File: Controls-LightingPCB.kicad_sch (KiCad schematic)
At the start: 30 parts, among them J1 PeripheralCANConnector, J2 PeripheralCANConnector, U1 PeripheralSOM

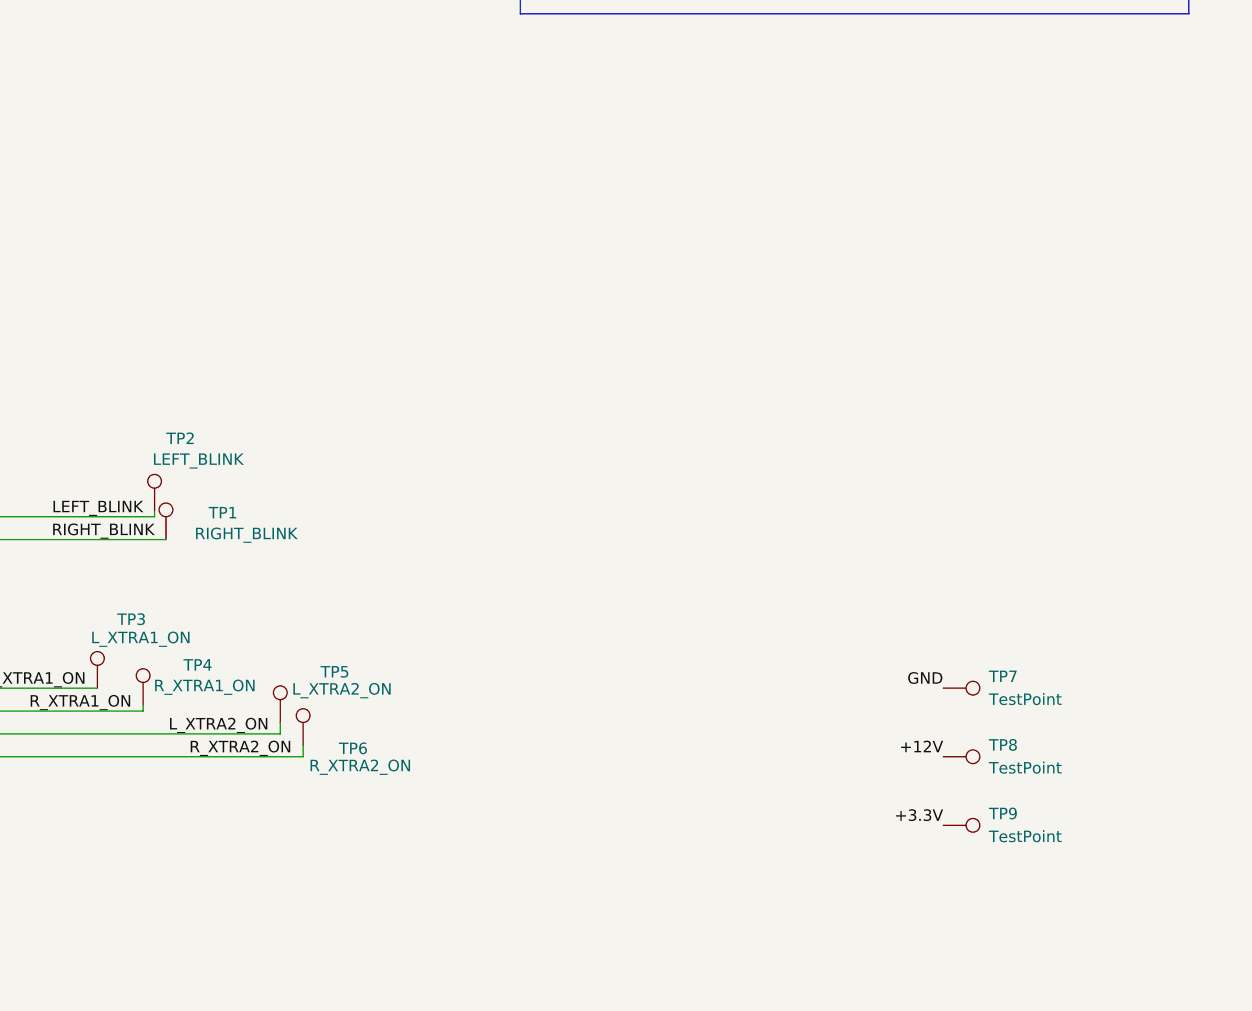
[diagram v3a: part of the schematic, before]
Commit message: added footprints for all components
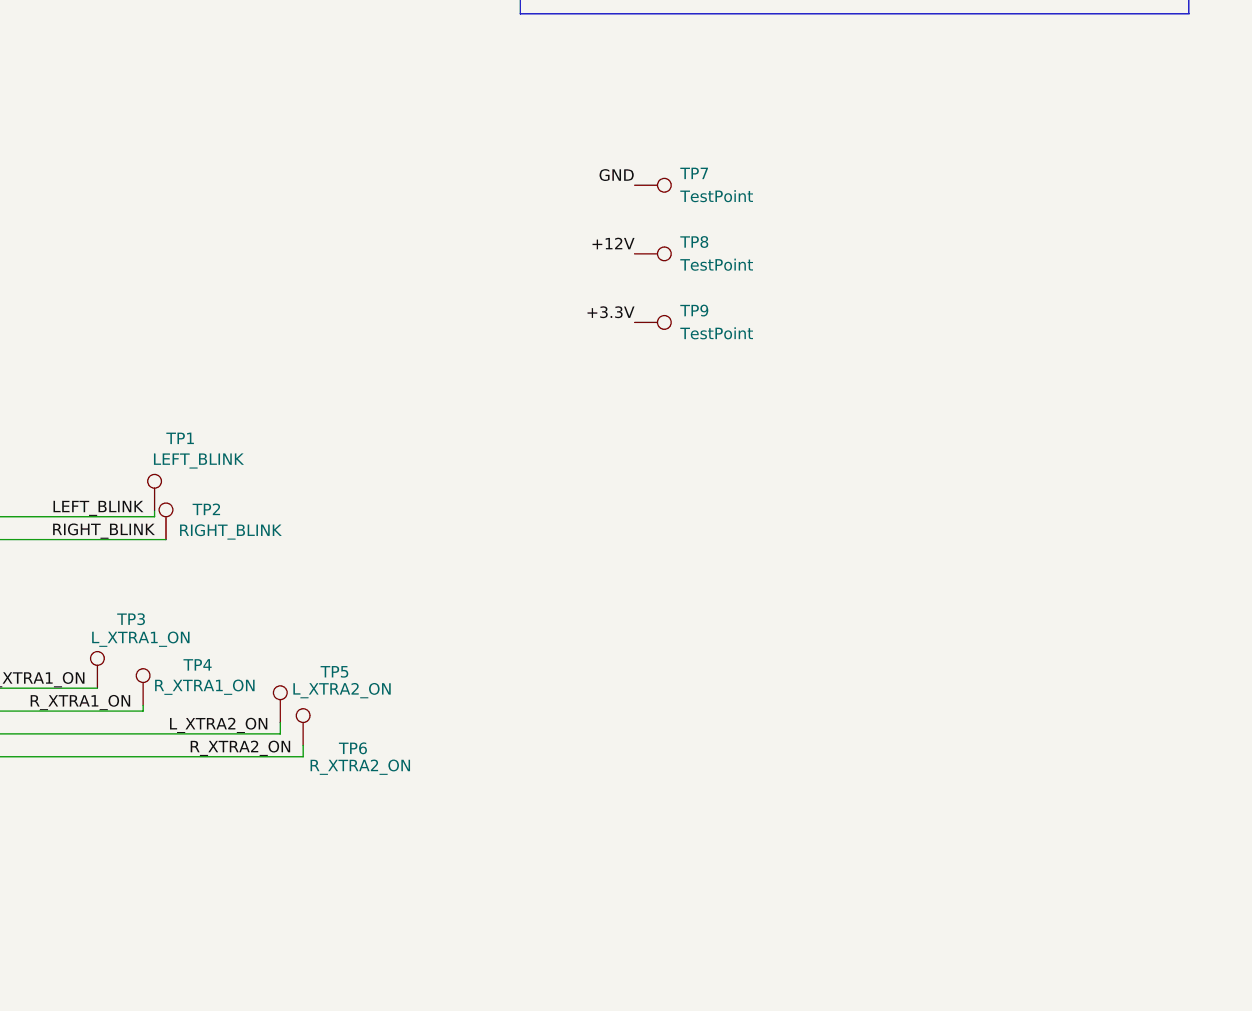
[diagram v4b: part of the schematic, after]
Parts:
- TP1: renamed from TP2; footprint TestPoint:TestPoint_Pad_1.5x1.5mm -> TestPoint:TestPoint_Keystone_5000-5004_Miniature
- TP2: renamed from TP1; footprint TestPoint:TestPoint_Pad_1.5x1.5mm -> TestPoint:TestPoint_Keystone_5000-5004_Miniature
- TP3, TP4, TP5, TP6: footprint TestPoint:TestPoint_Pad_1.5x1.5mm -> TestPoint:TestPoint_Keystone_5000-5004_Miniature
- TP7, TP8, TP9: footprint (none) -> TestPoint:TestPoint_Keystone_5000-5004_Miniature
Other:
- moved on the sheet: TP7, TP8, TP9
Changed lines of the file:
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@@
 	)
 	(label "+3.3V"
-		(at 251.46 140.97 180)
+		(at 217.17 85.09 180)
 		(fields_autoplaced yes)
 		(effects
@@
 	)
 	(label "+12V"
-		(at 251.46 133.35 180)
+		(at 217.17 77.47 180)
 		(fields_autoplaced yes)
 		(effects
@@
 	)
 	(label "GND"
-		(at 251.46 125.73 180)
+		(at 217.17 69.85 180)
 		(fields_autoplaced yes)
 		(effects
@@
 	(symbol
 		(lib_id "Connector:TestPoint")
-		(at 251.46 133.35 270)
+		(at 217.17 77.47 270)
 		(unit 1)
 		(exclude_from_sim no)
@@
 		(fields_autoplaced yes)
 		(property "Reference" "TP8"
-			(at 256.54 132.0799 90)
+			(at 222.25 76.1999 90)
 			(effects
 				(font
@@
 		)
 		(property "Value" "TestPoint"
-			(at 256.54 134.6199 90)
+			(at 222.25 78.7399 90)
 			(effects
 				(font
@@
 			)
 		)
-		(property "Footprint" ""
-			(at 251.46 138.43 0)
-			(effects
-				(font
-					(size 1.27 1.27)
-				)
-				(hide yes)
-			)
-		)
-		(property "Datasheet" "~"
-			(at 251.46 138.43 0)
-			(effects
-				(font
-					(size 1.27 1.27)
-				)
-				(hide yes)
-			)
-		)
-		(property "Description" "test point"
-			(at 251.46 133.35 0)
+		(property "Footprint" "TestPoint:TestPoint_Keystone_5000-5004_Miniature"
+			(at 217.17 82.55 0)
+			(effects
+				(font
+					(size 1.27 1.27)
+				)
+				(hide yes)
+			)
+		)
+		(property "Datasheet" "https://www.keyelco.com/userAssets/file/M65p56.pdf"
+			(at 217.17 82.55 0)
+			(effects
+				(font
+					(size 1.27 1.27)
+				)
+				(hide yes)
+			)
+		)
+		(property "Description" "through-hole test point mini"
+			(at 217.17 77.47 0)
 			(effects
 				(font
@@
 		(on_board yes)
 		(dnp no)
-		(property "Reference" "TP1"
-			(at 171.45 106.2736 0)
+		(property "Reference" "TP2"
+			(at 169.672 105.918 0)
 			(effects
 				(font
@@
 		)
 		(property "Value" "RIGHT_BLINK"
-			(at 173.99 108.585 0)
-			(effects
-				(font
-					(size 1.27 1.27)
-				)
-			)
-		)
-		(property "Footprint" "TestPoint:TestPoint_Pad_1.5x1.5mm"
+			(at 172.212 108.2294 0)
+			(effects
+				(font
+					(size 1.27 1.27)
+				)
+			)
+		)
+		(property "Footprint" "TestPoint:TestPoint_Keystone_5000-5004_Miniature"
 			(at 170.18 109.22 0)
 			(effects
@@
 			)
 		)
-		(property "Datasheet" "~"
+		(property "Datasheet" "https://www.keyelco.com/userAssets/file/M65p56.pdf"
 			(at 170.18 109.22 0)
 			(effects
@@
 			)
 		)
-		(property "Description" ""
+		(property "Description" "through-hole test point mini"
 			(at 165.1 109.22 0)
 			(effects
@@
 			(project "Controls-LightingPCB"
 				(path "/229b82f0-5048-47d6-8bc8-0bcee42eb4bc"
-					(reference "TP1")
+					(reference "TP2")
 					(unit 1)
 				)
@@
 			)
 		)
-		(property "Footprint" "TestPoint:TestPoint_Pad_1.5x1.5mm"
+		(property "Footprint" "TestPoint:TestPoint_Keystone_5000-5004_Miniature"
 			(at 167.64 127.635 0)
 			(effects
@@
 			)
 		)
-		(property "Datasheet" "~"
+		(property "Datasheet" "https://www.keyelco.com/userAssets/file/M65p56.pdf"
 			(at 167.64 127.635 0)
 			(effects
@@
 			)
 		)
-		(property "Description" ""
+		(property "Description" "through-hole test point mini"
 			(at 162.56 127.635 0)
 			(effects
@@
 			)
 		)
-		(property "Footprint" "TestPoint:TestPoint_Pad_1.5x1.5mm"
+		(property "Footprint" "TestPoint:TestPoint_Keystone_5000-5004_Miniature"
 			(at 162.56 125.73 0)
 			(effects
@@
 			)
 		)
-		(property "Datasheet" "~"
+		(property "Datasheet" "https://www.keyelco.com/userAssets/file/M65p56.pdf"
 			(at 162.56 125.73 0)
 			(effects
@@
 			)
 		)
-		(property "Description" ""
+		(property "Description" "through-hole test point mini"
 			(at 157.48 125.73 0)
 			(effects
@@
 		(on_board yes)
 		(dnp no)
-		(property "Reference" "TP2"
+		(property "Reference" "TP1"
 			(at 166.751 98.0186 0)
 			(effects
@@
 			)
 		)
-		(property "Footprint" "TestPoint:TestPoint_Pad_1.5x1.5mm"
+		(property "Footprint" "TestPoint:TestPoint_Keystone_5000-5004_Miniature"
 			(at 168.91 106.045 0)
 			(effects
@@
 			)
 		)
-		(property "Datasheet" "~"
+		(property "Datasheet" "https://www.keyelco.com/userAssets/file/M65p56.pdf"
 			(at 168.91 106.045 0)
 			(effects
@@
 			)
 		)
-		(property "Description" ""
+		(property "Description" "through-hole test point mini"
 			(at 163.83 106.045 0)
 			(effects
@@
 			(project "Controls-LightingPCB"
 				(path "/229b82f0-5048-47d6-8bc8-0bcee42eb4bc"
-					(reference "TP2")
+					(reference "TP1")
 					(unit 1)
 				)
@@
 			)
 		)
-		(property "Footprint" "TestPoint:TestPoint_Pad_1.5x1.5mm"
+		(property "Footprint" "TestPoint:TestPoint_Keystone_5000-5004_Miniature"
 			(at 182.88 129.54 0)
 			(effects
@@
 			)
 		)
-		(property "Datasheet" "~"
+		(property "Datasheet" "https://www.keyelco.com/userAssets/file/M65p56.pdf"
 			(at 182.88 129.54 0)
 			(effects
@@
 			)
 		)
-		(property "Description" ""
+		(property "Description" "through-hole test point mini"
 			(at 177.8 129.54 0)
 			(effects
@@
 	(symbol
 		(lib_id "Connector:TestPoint")
-		(at 251.46 125.73 270)
+		(at 217.17 69.85 270)
 		(unit 1)
 		(exclude_from_sim no)
@@
 		(fields_autoplaced yes)
 		(property "Reference" "TP7"
-			(at 256.54 124.4599 90)
+			(at 222.25 68.5799 90)
 			(effects
 				(font
@@
 		)
 		(property "Value" "TestPoint"
-			(at 256.54 126.9999 90)
+			(at 222.25 71.1199 90)
 			(effects
 				(font
@@
 			)
 		)
-		(property "Footprint" ""
-			(at 251.46 130.81 0)
-			(effects
-				(font
-					(size 1.27 1.27)
-				)
-				(hide yes)
-			)
-		)
-		(property "Datasheet" "~"
-			(at 251.46 130.81 0)
-			(effects
-				(font
-					(size 1.27 1.27)
-				)
-				(hide yes)
-			)
-		)
-		(property "Description" "test point"
-			(at 251.46 125.73 0)
+		(property "Footprint" "TestPoint:TestPoint_Keystone_5000-5004_Miniature"
+			(at 217.17 74.93 0)
+			(effects
+				(font
+					(size 1.27 1.27)
+				)
+				(hide yes)
+			)
+		)
+		(property "Datasheet" "https://www.keyelco.com/userAssets/file/M65p56.pdf"
+			(at 217.17 74.93 0)
+			(effects
+				(font
+					(size 1.27 1.27)
+				)
+				(hide yes)
+			)
+		)
+		(property "Description" "through-hole test point mini"
+			(at 217.17 69.85 0)
 			(effects
 				(font
@@
 	(symbol
 		(lib_id "Connector:TestPoint")
-		(at 251.46 140.97 270)
+		(at 217.17 85.09 270)
 		(unit 1)
 		(exclude_from_sim no)
@@
 		(fields_autoplaced yes)
 		(property "Reference" "TP9"
-			(at 256.54 139.6999 90)
+			(at 222.25 83.8199 90)
 			(effects
 				(font
@@
 		)
 		(property "Value" "TestPoint"
-			(at 256.54 142.2399 90)
+			(at 222.25 86.3599 90)
 			(effects
 				(font
@@
 			)
 		)
-		(property "Footprint" ""
-			(at 251.46 146.05 0)
-			(effects
-				(font
-					(size 1.27 1.27)
-				)
-				(hide yes)
-			)
-		)
-		(property "Datasheet" "~"
-			(at 251.46 146.05 0)
-			(effects
-				(font
-					(size 1.27 1.27)
-				)
-				(hide yes)
-			)
-		)
-		(property "Description" "test point"
-			(at 251.46 140.97 0)
+		(property "Footprint" "TestPoint:TestPoint_Keystone_5000-5004_Miniature"
+			(at 217.17 90.17 0)
+			(effects
+				(font
+					(size 1.27 1.27)
+				)
+				(hide yes)
+			)
+		)
+		(property "Datasheet" "https://www.keyelco.com/userAssets/file/M65p56.pdf"
+			(at 217.17 90.17 0)
+			(effects
+				(font
+					(size 1.27 1.27)
+				)
+				(hide yes)
+			)
+		)
+		(property "Description" "through-hole test point mini"
+			(at 217.17 85.09 0)
 			(effects
 				(font
@@
 			)
 		)
-		(property "Footprint" "TestPoint:TestPoint_Pad_1.5x1.5mm"
+		(property "Footprint" "TestPoint:TestPoint_Keystone_5000-5004_Miniature"
 			(at 185.42 132.08 0)
 			(effects
@@
 			)
 		)
-		(property "Datasheet" "~"
+		(property "Datasheet" "https://www.keyelco.com/userAssets/file/M65p56.pdf"
 			(at 185.42 132.08 0)
 			(effects
@@
 			)
 		)
-		(property "Description" ""
+		(property "Description" "through-hole test point mini"
 			(at 180.34 132.08 0)
 			(effects

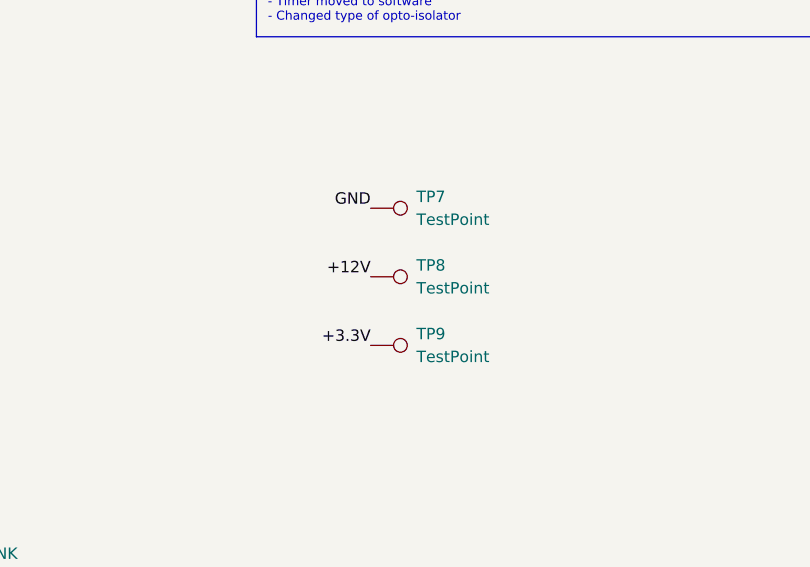
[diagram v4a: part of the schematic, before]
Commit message: changed lights resistor values and updated EL2H7 footprint
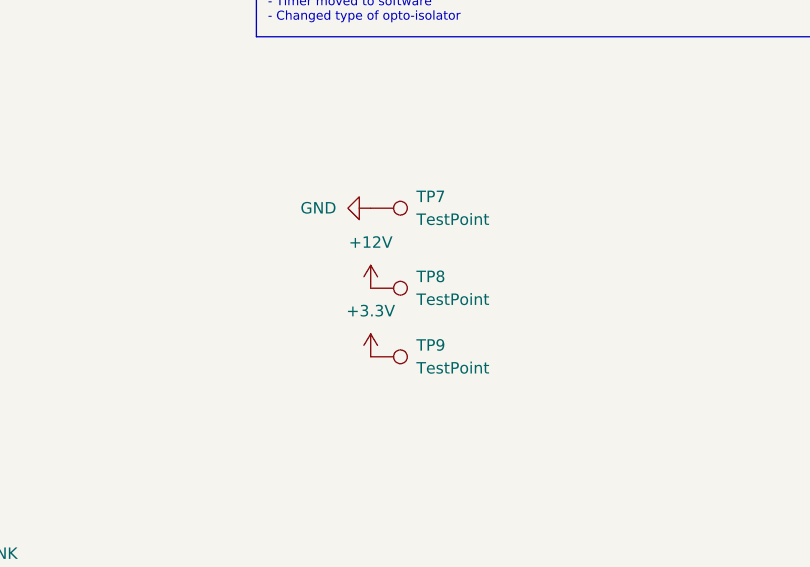
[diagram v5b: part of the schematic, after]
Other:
- moved on the sheet: TP8, TP9
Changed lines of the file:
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@@
 		)
 	)
-	(label "+3.3V"
-		(at 217.17 85.09 180)
-		(fields_autoplaced yes)
-		(effects
-			(font
-				(size 1.27 1.27)
-			)
-			(justify right bottom)
-		)
-	)
-	(label "+12V"
-		(at 217.17 77.47 180)
-		(fields_autoplaced yes)
-		(effects
-			(font
-				(size 1.27 1.27)
-			)
-			(justify right bottom)
-		)
-	)
 	(label "R_XTRA2_ON"
 		(at 179.07 133.35 180)
@@
 		)
 	)
-	(label "GND"
-		(at 217.17 69.85 180)
-		(fields_autoplaced yes)
-		(effects
-			(font
-				(size 1.27 1.27)
-			)
-			(justify right bottom)
-		)
-	)
 	(label "L_XTRA2_ON"
 		(at 96.52 157.48 0)
@@
 	(symbol
 		(lib_id "Connector:TestPoint")
-		(at 217.17 77.47 270)
+		(at 217.17 78.74 270)
 		(unit 1)
 		(exclude_from_sim no)
@@
 		(fields_autoplaced yes)
 		(property "Reference" "TP8"
-			(at 222.25 76.1999 90)
+			(at 222.25 77.4699 90)
 			(effects
 				(font
@@
 		)
 		(property "Value" "TestPoint"
-			(at 222.25 78.7399 90)
+			(at 222.25 80.0099 90)
 			(effects
 				(font
@@
 		)
 		(property "Footprint" "TestPoint:TestPoint_Keystone_5000-5004_Miniature"
-			(at 217.17 82.55 0)
+			(at 217.17 83.82 0)
 			(effects
 				(font
@@
 		)
 		(property "Datasheet" "https://www.keyelco.com/userAssets/file/M65p56.pdf"
-			(at 217.17 82.55 0)
+			(at 217.17 83.82 0)
 			(effects
 				(font
@@
 		)
 		(property "Description" "through-hole test point mini"
-			(at 217.17 77.47 0)
+			(at 217.17 78.74 0)
 			(effects
 				(font
@@
 	)
 	(symbol
+		(lib_id "power:+3.3V")
+		(at 217.17 86.36 0)
+		(unit 1)
+		(exclude_from_sim no)
+		(in_bom yes)
+		(on_board yes)
+		(dnp no)
+		(fields_autoplaced yes)
+		(property "Reference" "#PWR031"
+			(at 217.17 90.17 0)
+			(effects
+				(font
+					(size 1.27 1.27)
+				)
+				(hide yes)
+			)
+		)
+		(property "Value" "+3.3V"
+			(at 217.17 81.28 0)
+			(effects
+				(font
+					(size 1.27 1.27)
+				)
+			)
+		)
+		(property "Footprint" ""
+			(at 217.17 86.36 0)
+			(effects
+				(font
+					(size 1.27 1.27)
+				)
+				(hide yes)
+			)
+		)
+		(property "Datasheet" ""
+			(at 217.17 86.36 0)
+			(effects
+				(font
+					(size 1.27 1.27)
+				)
+				(hide yes)
+			)
+		)
+		(property "Description" "Power symbol creates a global label with name \"+3.3V\""
+			(at 217.17 86.36 0)
+			(effects
+				(font
+					(size 1.27 1.27)
+				)
+				(hide yes)
+			)
+		)
+		(pin "1"
+		)
+		(instances
+			(project ""
+				(path "/229b82f0-5048-47d6-8bc8-0bcee42eb4bc"
+					(reference "#PWR031")
+					(unit 1)
+				)
+			)
+		)
+	)
+	(symbol
 		(lib_id "power:GNDPWR")
 		(at 78.74 125.73 270)
@@
 	)
 	(symbol
+		(lib_id "power:+12V")
+		(at 217.17 78.74 0)
+		(unit 1)
+		(exclude_from_sim no)
+		(in_bom yes)
+		(on_board yes)
+		(dnp no)
+		(fields_autoplaced yes)
+		(property "Reference" "#PWR030"
+			(at 217.17 82.55 0)
+			(effects
+				(font
+					(size 1.27 1.27)
+				)
+				(hide yes)
+			)
+		)
+		(property "Value" "+12V"
+			(at 217.17 73.66 0)
+			(effects
+				(font
+					(size 1.27 1.27)
+				)
+			)
+		)
+		(property "Footprint" ""
+			(at 217.17 78.74 0)
+			(effects
+				(font
+					(size 1.27 1.27)
+				)
+				(hide yes)
+			)
+		)
+		(property "Datasheet" ""
+			(at 217.17 78.74 0)
+			(effects
+				(font
+					(size 1.27 1.27)
+				)
+				(hide yes)
+			)
+		)
+		(property "Description" "Power symbol creates a global label with name \"+12V\""
+			(at 217.17 78.74 0)
+			(effects
+				(font
+					(size 1.27 1.27)
+				)
+				(hide yes)
+			)
+		)
+		(pin "1"
+		)
+		(instances
+			(project ""
+				(path "/229b82f0-5048-47d6-8bc8-0bcee42eb4bc"
+					(reference "#PWR030")
+					(unit 1)
+				)
+			)
+		)
+	)
+	(symbol
 		(lib_id "power:GND")
 		(at 34.29 180.34 0)
@@
 	(symbol
 		(lib_id "Connector:TestPoint")
-		(at 217.17 85.09 270)
+		(at 217.17 86.36 270)
 		(unit 1)
 		(exclude_from_sim no)
@@
 		(fields_autoplaced yes)
 		(property "Reference" "TP9"
-			(at 222.25 83.8199 90)
+			(at 222.25 85.0899 90)
 			(effects
 				(font
@@
 		)
 		(property "Value" "TestPoint"
-			(at 222.25 86.3599 90)
+			(at 222.25 87.6299 90)
 			(effects
 				(font
@@
 		)
 		(property "Footprint" "TestPoint:TestPoint_Keystone_5000-5004_Miniature"
-			(at 217.17 90.17 0)
+			(at 217.17 91.44 0)
 			(effects
 				(font
@@
 		)
 		(property "Datasheet" "https://www.keyelco.com/userAssets/file/M65p56.pdf"
-			(at 217.17 90.17 0)
+			(at 217.17 91.44 0)
 			(effects
 				(font
@@
 		)
 		(property "Description" "through-hole test point mini"
-			(at 217.17 85.09 0)
+			(at 217.17 86.36 0)
 			(effects
 				(font
@@
 	(symbol
 		(lib_id "power:GND")
+		(at 217.17 69.85 270)
+		(unit 1)
+		(exclude_from_sim no)
+		(in_bom yes)
+		(on_board yes)
+		(dnp no)
+		(fields_autoplaced yes)
+		(property "Reference" "#PWR032"
+			(at 210.82 69.85 0)
+			(effects
+				(font
+					(size 1.27 1.27)
+				)
+				(hide yes)
+			)
+		)
+		(property "Value" "GND"
+			(at 213.36 69.8499 90)
+			(effects
+				(font
+					(size 1.27 1.27)
+				)
+				(justify right)
+			)
+		)
+		(property "Footprint" ""
+			(at 217.17 69.85 0)
+			(effects
+				(font
+					(size 1.27 1.27)
+				)
+				(hide yes)
+			)
+		)
+		(property "Datasheet" ""
+			(at 217.17 69.85 0)
+			(effects
+				(font
+					(size 1.27 1.27)
+				)
+				(hide yes)
+			)
+		)
+		(property "Description" "Power symbol creates a global label with name \"GND\" , ground"
+			(at 217.17 69.85 0)
+			(effects
+				(font
+					(size 1.27 1.27)
+				)
+				(hide yes)
+			)
+		)
+		(pin "1"
+		)
+		(instances
+			(project ""
+				(path "/229b82f0-5048-47d6-8bc8-0bcee42eb4bc"
+					(reference "#PWR032")
+					(unit 1)
+				)
+			)
+		)
+	)
+	(symbol
+		(lib_id "power:GND")
 		(at 96.52 180.34 0)
 		(unit 1)
@@
 			)
 		)
-		(property "Description" ""
+		(property "Description" "peripheral som connector"
 			(at 109.22 83.82 0)
 			(effects

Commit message: updated prelim
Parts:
- R13, R14, R15, R16, R17, R18: value 698 -> 1k
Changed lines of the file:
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@@
 			)
 		)
-		(property "Value" "698"
+		(property "Value" "1k"
 			(at 113.538 167.513 0)
 			(effects
@@
 			)
 		)
-		(property "Value" "698"
+		(property "Value" "1k"
 			(at 52.578 167.513 0)
 			(effects
@@
 			)
 		)
-		(property "Value" "698"
+		(property "Value" "1k"
 			(at 36.068 167.513 0)
 			(effects
@@
 			)
 		)
-		(property "Value" "698"
+		(property "Value" "1k"
 			(at 67.818 167.513 0)
 			(effects
@@
 			)
 		)
-		(property "Value" "698"
+		(property "Value" "1k"
 			(at 83.058 167.513 0)
 			(effects
@@
 			)
 		)
-		(property "Value" "698"
+		(property "Value" "1k"
 			(at 98.298 167.513 0)
 			(effects
